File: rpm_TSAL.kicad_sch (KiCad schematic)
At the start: 2 parts, among them J1 Conn_01x02, J5 Conn_01x02

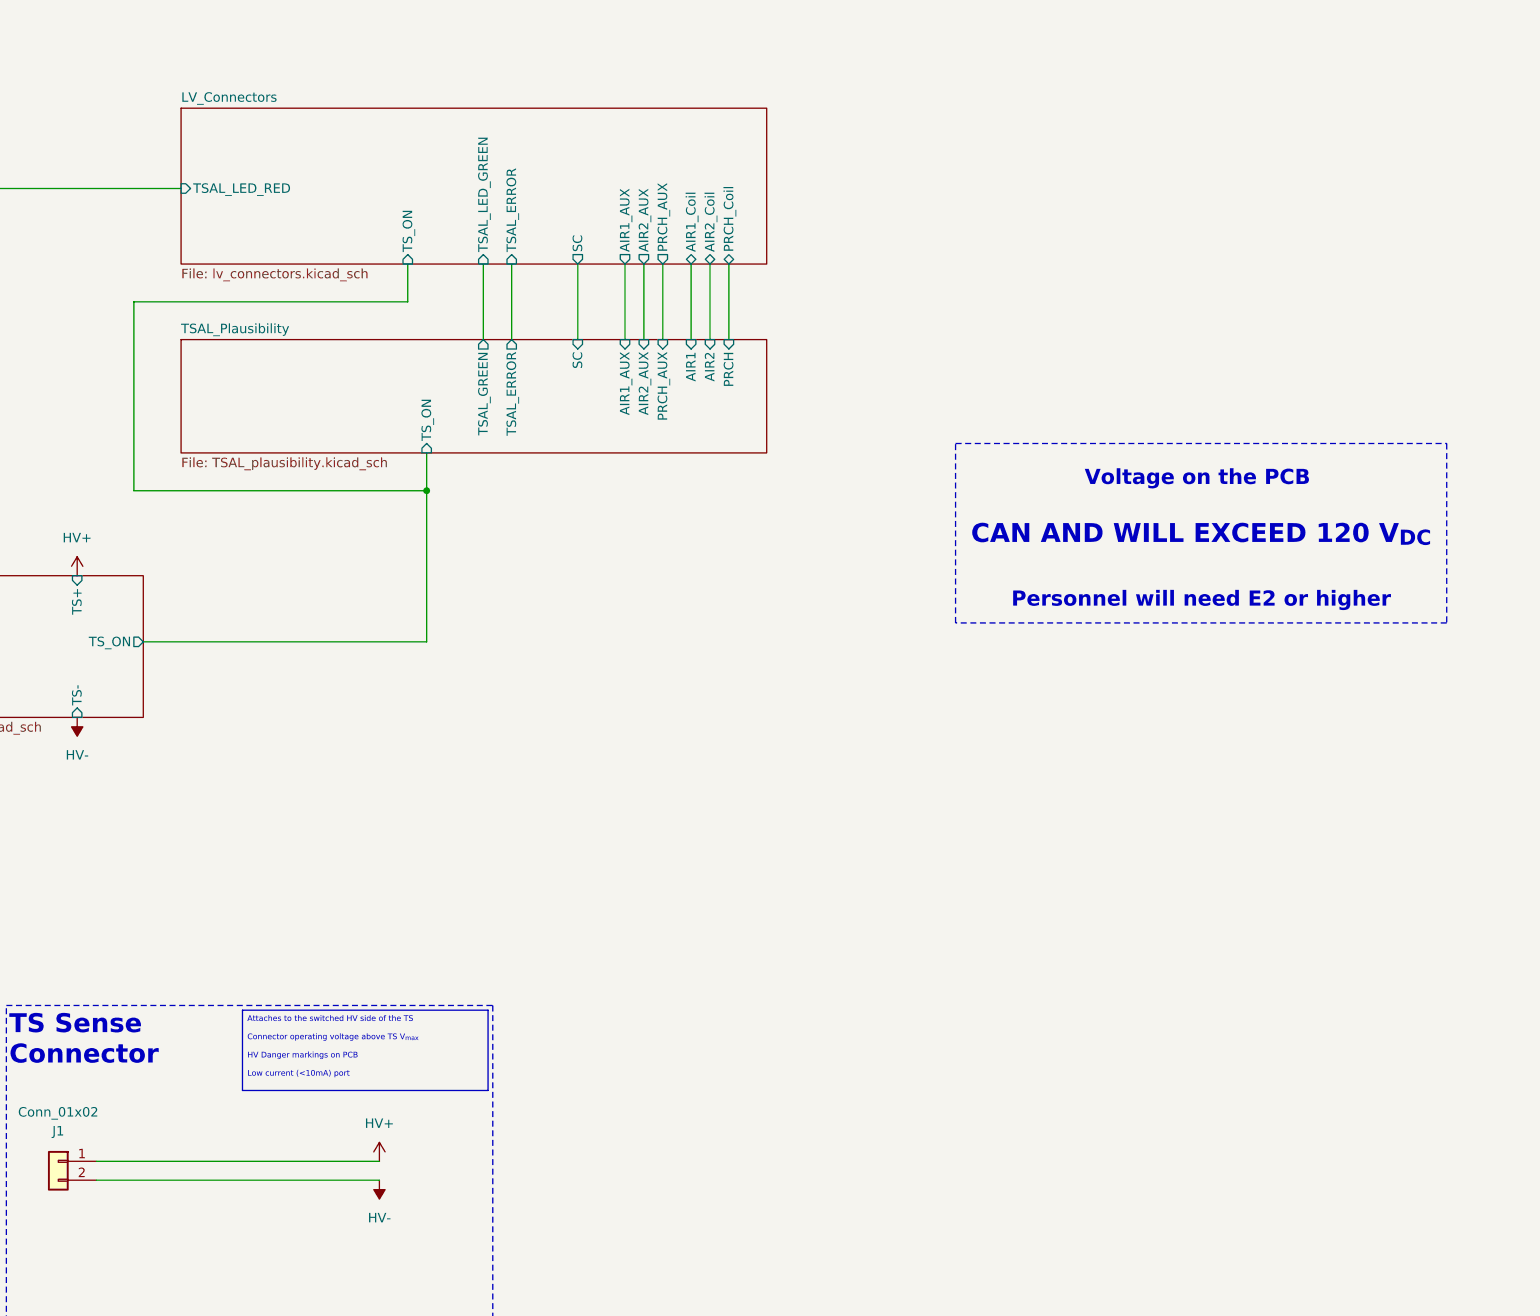
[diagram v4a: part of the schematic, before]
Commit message: Added new Subsheet
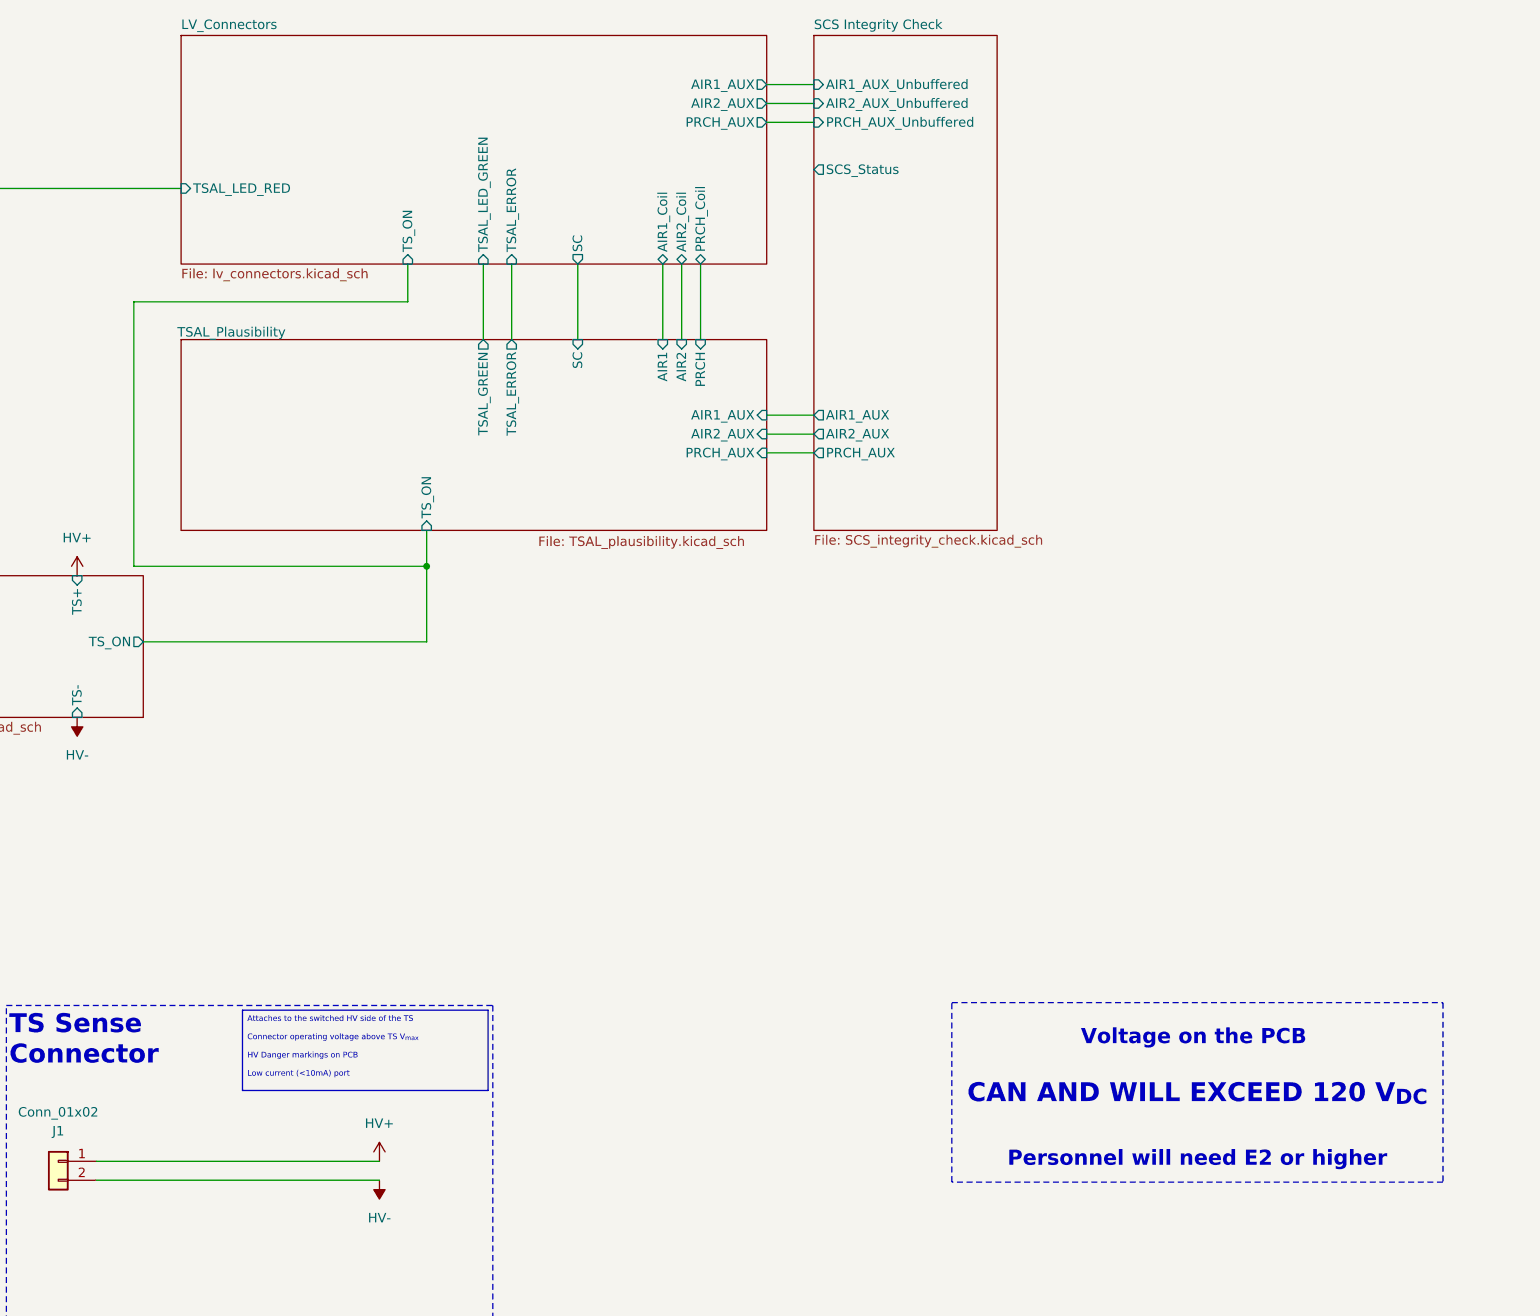
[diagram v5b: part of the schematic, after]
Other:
- added sheet SCS Integrity Check (SCS_integrity_check.kicad_sch)
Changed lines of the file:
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@@
 	)
 	(junction
-		(at 147.32 78.74)
+		(at 147.32 88.9)
 		(diameter 0)
 		(color 0 0 0 0)
@@
 	(wire
 		(pts
-			(xy 147.32 78.74) (xy 107.95 78.74)
+			(xy 147.32 88.9) (xy 107.95 88.9)
 		)
 		(stroke
@@
 	(wire
 		(pts
-			(xy 187.96 48.26) (xy 187.96 58.42)
+			(xy 184.15 48.26) (xy 184.15 58.42)
 		)
 		(stroke
@@
 	(wire
 		(pts
-			(xy 107.95 78.74) (xy 107.95 53.34)
+			(xy 147.32 88.9) (xy 147.32 84.074)
+		)
+		(stroke
+			(width 0)
+			(type default)
+		)
+	)
+	(wire
+		(pts
+			(xy 107.95 88.9) (xy 107.95 53.34)
+		)
+		(stroke
+			(width 0)
+			(type default)
+		)
+	)
+	(wire
+		(pts
+			(xy 193.04 26.67) (xy 199.39 26.67)
 		)
 		(stroke
@@
 	(wire
 		(pts
-			(xy 185.42 48.26) (xy 185.42 58.42)
+			(xy 181.61 48.26) (xy 181.61 58.42)
 		)
 		(stroke
@@
 	(wire
 		(pts
-			(xy 182.88 48.26) (xy 182.88 58.42)
+			(xy 179.07 48.26) (xy 179.07 58.42)
 		)
 		(stroke
@@
 	(wire
 		(pts
-			(xy 179.07 48.26) (xy 179.07 58.42)
+			(xy 147.32 99.06) (xy 147.32 88.9)
 		)
 		(stroke
@@
 	(wire
 		(pts
-			(xy 147.32 99.06) (xy 147.32 78.74)
+			(xy 193.04 29.21) (xy 199.39 29.21)
 		)
 		(stroke
@@
 	(wire
 		(pts
-			(xy 173.99 48.26) (xy 173.99 58.42)
-		)
-		(stroke
-			(width 0)
-			(type default)
-		)
-	)
-	(wire
-		(pts
 			(xy 34.29 171.45) (xy 73.66 171.45)
 		)
@@
 	(wire
 		(pts
-			(xy 147.32 78.74) (xy 147.32 73.66)
+			(xy 193.04 71.12) (xy 199.39 71.12)
+		)
+		(stroke
+			(width 0)
+			(type default)
+		)
+	)
+	(wire
+		(pts
+			(xy 193.04 73.66) (xy 199.39 73.66)
+		)
+		(stroke
+			(width 0)
+			(type default)
+		)
+	)
+	(wire
+		(pts
+			(xy 193.04 24.13) (xy 199.39 24.13)
 		)
 		(stroke
@@
 	(wire
 		(pts
+			(xy 193.04 68.58) (xy 199.39 68.58)
+		)
+		(stroke
+			(width 0)
+			(type default)
+		)
+	)
+	(wire
+		(pts
 			(xy 167.64 48.26) (xy 167.64 58.42)
 		)
@@
 		)
 	)
-	(wire
-		(pts
-			(xy 176.53 48.26) (xy 176.53 58.42)
-		)
-		(stroke
-			(width 0)
-			(type default)
-		)
-	)
 	(rectangle
 		(start 22.225 147.955)
@@
 	)
 	(image
-		(at 251.46 41.91)
+		(at 250.952 117.094)
 		(scale 0.768822)
 		(data "iVBORw0KGgoAAAANSUhEUgAABAAAAAN/CAYAAABAzqoZAAAABGdBTUEAALGPC/xhBQAAACBjSFJN"
@@
 	(text_box "_{Voltage on the PCB }\n\nCAN AND WILL EXCEED 120 V_{DC}\n\n_{Personnel will need E2 or higher}"
 		(exclude_from_sim no)
-		(at 218.44 72.39 0)
+		(at 217.932 147.574 0)
 		(size 66.04 24.13)
 		(stroke
@@
 	(sheet
 		(at 114.3 58.42)
-		(size 78.74 15.24)
-		(fields_autoplaced yes)
+		(size 78.74 25.654)
 		(stroke
 			(width 0.1524)
@@
 		)
 		(property "Sheetname" "TSAL_Plausibility"
-			(at 114.3 57.7084 0)
+			(at 113.792 58.166 0)
 			(effects
 				(font
@@
 		)
 		(property "Sheetfile" "TSAL_plausibility.kicad_sch"
-			(at 114.3 74.2446 0)
+			(at 162.306 84.836 0)
 			(effects
 				(font
@@
 		)
 		(pin "AIR2" input
-			(at 185.42 58.42 90)
+			(at 181.61 58.42 90)
 			(effects
 				(font
@@
 		)
 		(pin "AIR1" input
-			(at 182.88 58.42 90)
+			(at 179.07 58.42 90)
 			(effects
 				(font
@@
 		)
 		(pin "PRCH" input
-			(at 187.96 58.42 90)
+			(at 184.15 58.42 90)
 			(effects
 				(font
@@
 		)
 		(pin "AIR1_AUX" input
-			(at 173.99 58.42 90)
+			(at 193.04 68.58 0)
 			(effects
 				(font
@@
 		)
 		(pin "AIR2_AUX" input
-			(at 176.53 58.42 90)
+			(at 193.04 71.12 0)
 			(effects
 				(font
@@
 		)
 		(pin "TS_ON" input
-			(at 147.32 73.66 270)
+			(at 147.32 84.074 270)
 			(effects
 				(font
@@
 		)
 		(pin "PRCH_AUX" input
-			(at 179.07 58.42 90)
+			(at 193.04 73.66 0)
 			(effects
 				(font
@@
 	)
 	(sheet
+		(at 199.39 17.526)
+		(size 24.638 66.548)
+		(fields_autoplaced yes)
+		(stroke
+			(width 0.1524)
+			(type solid)
+		)
+		(fill
+			(color 0 0 0 0.0000)
+		)
+		(property "Sheetname" "SCS Integrity Check"
+			(at 199.39 16.8144 0)
+			(effects
+				(font
+					(size 1.27 1.27)
+				)
+				(justify left bottom)
+			)
+		)
+		(property "Sheetfile" "SCS_integrity_check.kicad_sch"
+			(at 199.39 84.6586 0)
+			(effects
+				(font
+					(size 1.27 1.27)
+				)
+				(justify left top)
+			)
+		)
+		(pin "SCS_Status" output
+			(at 199.39 35.56 180)
+			(effects
+				(font
+					(size 1.27 1.27)
+				)
+				(justify left)
+			)
+		)
+		(pin "PRCH_AUX" output
+			(at 199.39 73.66 180)
+			(effects
+				(font
+					(size 1.27 1.27)
+				)
+				(justify left)
+			)
+		)
+		(pin "AIR2_AUX" output
+			(at 199.39 71.12 180)
+			(effects
+				(font
+					(size 1.27 1.27)
+				)
+				(justify left)
+			)
+		)
+		(pin "PRCH_AUX_Unbuffered" input
+			(at 199.39 29.21 180)
+			(effects
+				(font
+					(size 1.27 1.27)
+				)
+				(justify left)
+			)
+		)
+		(pin "AIR1_AUX" output
+			(at 199.39 68.58 180)
+			(effects
+				(font
+					(size 1.27 1.27)
+				)
+				(justify left)
+			)
+		)
+		(pin "AIR1_AUX_Unbuffered" input
+			(at 199.39 24.13 180)
+			(effects
+				(font
+					(size 1.27 1.27)
+				)
+				(justify left)
+			)
+		)
+		(pin "AIR2_AUX_Unbuffered" input
+			(at 199.39 26.67 180)
+			(effects
+				(font
+					(size 1.27 1.27)
+				)
+				(justify left)
+			)
+		)
+		(instances
+			(project "rpm_TSAL"
+				(path "/d61aec95-1a95-4bdc-98ef-7f05cebfb826"
+					(page "4")
+				)
+			)
+		)
+	)
+	(sheet
 		(at 74.295 90.17)
 		(size 34.925 19.05)
@@
 	)
 	(sheet
-		(at 114.3 27.305)
-		(size 78.74 20.955)
+		(at 114.3 17.526)
+		(size 78.74 30.734)
 		(fields_autoplaced yes)
 		(stroke
@@
 		)
 		(property "Sheetname" "LV_Connectors"
-			(at 114.3 26.5934 0)
+			(at 114.3 16.8144 0)
 			(effects
 				(font
@@
 			)
 		)
-		(pin "PRCH_AUX" output
-			(at 179.07 48.26 270)
-			(effects
-				(font
-					(size 1.27 1.27)
-				)
-				(justify left)
-			)
-		)
 		(pin "SC" output
 			(at 167.64 48.26 270)
@@
 			)
 		)
-		(pin "AIR2_AUX" output
-			(at 176.53 48.26 270)
-			(effects
-				(font
-					(size 1.27 1.27)
-				)
-				(justify left)
-			)
-		)
-		(pin "AIR1_AUX" output
-			(at 173.99 48.26 270)
-			(effects
-				(font
-					(size 1.27 1.27)
-				)
-				(justify left)
-			)
-		)
 		(pin "TS_ON" input
 			(at 144.78 48.26 270)
@@
 		)
 		(pin "AIR2_Coil" bidirectional
-			(at 185.42 48.26 270)
+			(at 181.61 48.26 270)
 			(effects
 				(font
@@
 		)
 		(pin "AIR1_Coil" bidirectional
-			(at 182.88 48.26 270)
+			(at 179.07 48.26 270)
 			(effects
 				(font
@@
 		)
 		(pin "PRCH_Coil" bidirectional
-			(at 187.96 48.26 270)
+			(at 184.15 48.26 270)
 			(effects
 				(font
@@
 				)
 				(justify left)
+			)
+		)
+		(pin "AIR2_AUX" output
+			(at 193.04 26.67 0)
+			(effects
+				(font
+					(size 1.27 1.27)
+				)
+				(justify right)
+			)
+		)
+		(pin "AIR1_AUX" output
+			(at 193.04 24.13 0)
+			(effects
+				(font
+					(size 1.27 1.27)
+				)
+				(justify right)
+			)
+		)
+		(pin "PRCH_AUX" output
+			(at 193.04 29.21 0)
+			(effects
+				(font
+					(size 1.27 1.27)
+				)
+				(justify right)
 			)
 		)
@@
 			(project "rpm_TSAL"
 				(path "/d61aec95-1a95-4bdc-98ef-7f05cebfb826"
-					(page "4")
-				)
-			)
+					(page "6")
+				)
+			)
